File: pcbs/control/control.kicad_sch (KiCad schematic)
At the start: 57 parts, among them J2 USB4125-GF-A-0190, J3 Conn_01x10_Pin, J4 Conn_02x04_Odd_Even, Q1 PMV35EPER, Q10 DMN2020LSN-7, Q2 PMV35EPER, Q3 PMV35EPER, Q4 PMV35EPER, Q5 DMN2020LSN-7, Q6 DMN2020LSN-7, Q7 DMN2020LSN-7, Q8 DMN2020LSN-7, Q9 DMN2020LSN-7, SW1 Sparkle Btn, SW2 Time Adj Btn, U1 DS18B20U, U2 DS3231MZ, U3 TPS259620, U6 ATmega328PB-A

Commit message: pcb and enclosure update
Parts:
- removed BT1: 3000TR, Clock:BAT_3000TR, symbol Clock:3000TR
- added J1: Conn_01x02_Pin, Connector_JST:JST_PH_S2B-PH-SM4-TB_1x02-1MP_P2.00mm_Horizontal, symbol Connector:Conn_01x02_Pin
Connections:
- net GNDD: now also J1.1 (Pin_1)
- net RTC_BAT: now also J1.2 (Pin_2)

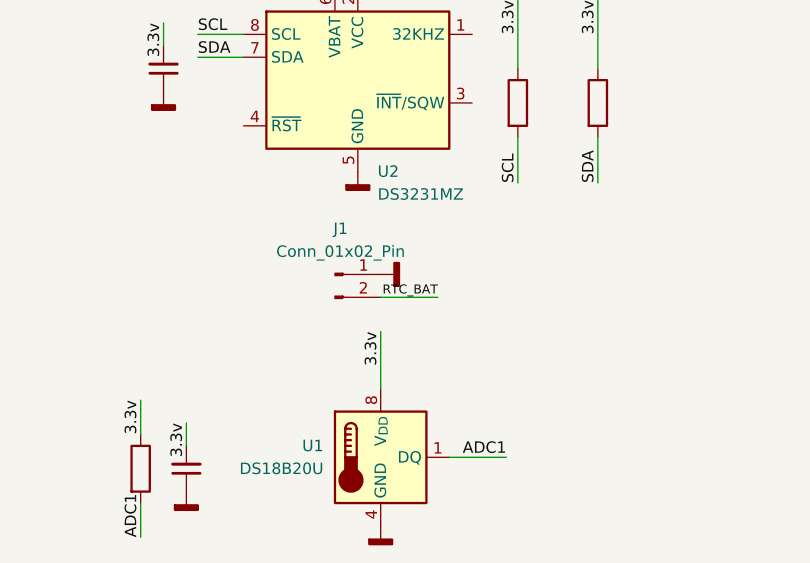
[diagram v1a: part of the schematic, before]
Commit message: lengthened display cable
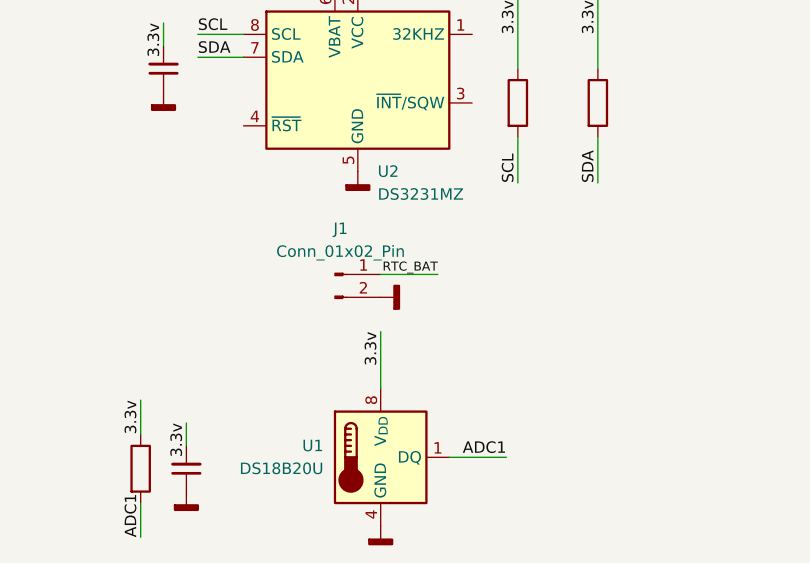
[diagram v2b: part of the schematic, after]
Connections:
- net GNDD: now also J1.2 (Pin_2); no longer J1.1 (Pin_1)
- net RTC_BAT: now also J1.1 (Pin_1); no longer J1.2 (Pin_2)
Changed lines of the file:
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@@
 	(wire
 		(pts
-			(xy 41.91 158.75) (xy 46.99 158.75)
+			(xy 127 153.67) (xy 133.35 153.67)
 		)
 		(stroke
@@
 	(wire
 		(pts
-			(xy 78.74 39.37) (xy 78.74 41.91)
+			(xy 41.91 158.75) (xy 46.99 158.75)
 		)
 		(stroke
@@
 	(wire
 		(pts
-			(xy 137.16 91.44) (xy 143.51 91.44)
+			(xy 78.74 39.37) (xy 78.74 41.91)
 		)
 		(stroke
@@
 	(wire
 		(pts
-			(xy 186.69 66.04) (xy 189.23 66.04)
+			(xy 137.16 91.44) (xy 143.51 91.44)
 		)
 		(stroke
@@
 	(wire
 		(pts
-			(xy 124.46 114.3) (xy 124.46 121.92)
+			(xy 186.69 66.04) (xy 189.23 66.04)
 		)
 		(stroke
@@
 	(wire
 		(pts
-			(xy 127 156.21) (xy 133.35 156.21)
+			(xy 124.46 114.3) (xy 124.46 121.92)
 		)
 		(stroke
@@
 		)
 	)
-	(label "RTC_BAT"
-		(at 133.35 156.21 180)
-		(fields_autoplaced yes)
-		(effects
-			(font
-				(size 1 1)
-			)
-			(justify right bottom)
-		)
-	)
 	(label "ADC3"
 		(at 143.51 66.04 180)
@@
 		)
 	)
+	(label "RTC_BAT"
+		(at 133.35 153.67 180)
+		(fields_autoplaced yes)
+		(effects
+			(font
+				(size 1 1)
+			)
+			(justify right bottom)
+		)
+	)
 	(label "5v"
 		(at 82.55 109.22 270)
@@
 	)
 	(symbol
-		(lib_id "power:GNDD")
-		(at 127 153.67 90)
-		(unit 1)
-		(exclude_from_sim no)
-		(in_bom yes)
-		(on_board yes)
-		(dnp no)
-		(fields_autoplaced yes)
-		(property "Reference" "#PWR026"
-			(at 133.35 153.67 0)
-			(effects
-				(font
-					(size 1.27 1.27)
-				)
-				(hide yes)
-			)
-		)
-		(property "Value" "GNDD"
-			(at 130.81 153.67 0)
-			(effects
-				(font
-					(size 1.27 1.27)
-				)
-				(hide yes)
-			)
-		)
-		(property "Footprint" ""
-			(at 127 153.67 0)
-			(effects
-				(font
-					(size 1.27 1.27)
-				)
-				(hide yes)
-			)
-		)
-		(property "Datasheet" ""
-			(at 127 153.67 0)
-			(effects
-				(font
-					(size 1.27 1.27)
-				)
-				(hide yes)
-			)
-		)
-		(property "Description" "Power symbol creates a global label with name \"GNDD\" , digital ground"
-			(at 127 153.67 0)
-			(effects
-				(font
-					(size 1.27 1.27)
-				)
-				(hide yes)
-			)
-		)
-		(pin "1"
-		)
-		(instances
-			(project "control"
-				(path "/6120ad7c-5b3a-4aa8-9b13-74a3f0996cb1"
-					(reference "#PWR026")
-					(unit 1)
-				)
-			)
-		)
-	)
-	(symbol
 		(lib_id "Device:C_Small")
 		(at 82.55 114.3 180)
@@
 					(unit 1)
 				)
+			)
+		)
+	)
+	(symbol
+		(lib_id "power:GNDD")
+		(at 127 156.21 90)
+		(unit 1)
+		(exclude_from_sim no)
+		(in_bom yes)
+		(on_board yes)
+		(dnp no)
+		(fields_autoplaced yes)
+		(property "Reference" "#PWR026"
+			(at 133.35 156.21 0)
+			(effects
+				(font
+					(size 1.27 1.27)
+				)
+				(hide yes)
+			)
+		)
+		(property "Value" "GNDD"
+			(at 130.81 156.21 0)
+			(effects
+				(font
+					(size 1.27 1.27)
+				)
+				(hide yes)
+			)
+		)
+		(property "Footprint" ""
+			(at 127 156.21 0)
+			(effects
+				(font
+					(size 1.27 1.27)
+				)
+				(hide yes)
+			)
+		)
+		(property "Datasheet" ""
+			(at 127 156.21 0)
+			(effects
+				(font
+					(size 1.27 1.27)
+				)
+				(hide yes)
+			)
+		)
+		(property "Description" "Power symbol creates a global label with name \"GNDD\" , digital ground"
+			(at 127 156.21 0)
+			(effects
+				(font
+					(size 1.27 1.27)
+				)
+				(hide yes)
+			)
+		)
+		(pin "1"
+		)
+		(instances
+			(project "control"
+				(path "/6120ad7c-5b3a-4aa8-9b13-74a3f0996cb1"
+					(reference "#PWR026")
+					(unit 1)
+				)

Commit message: rv-3028 board
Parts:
- removed J1: Conn_01x02_Pin, Connector_JST:JST_PH_S2B-PH-SM4-TB_1x02-1MP_P2.00mm_Horizontal, symbol Connector:Conn_01x02_Pin
- removed R19: 500, Resistor_SMD:R_0805_2012Metric, symbol Device:R
- removed R21, R22: 400k, Resistor_SMD:R_0805_2012Metric, symbol Device:R
- removed U2: DS3231MZ, Package_SO:SOIC-8_3.9x4.9mm_P1.27mm, symbol Timer_RTC:DS3231MZ
- removed U3: TPS259620, Clock:IC_TPS259621DDAT, symbol Clock:TPS259621DDAT
- added C8, C9: FC0V224ZFTBR24, Clock:CAPAE1080X550N, symbol Clock:FC0V224ZFTBR24
- added IC1: TPS25944LRVCR, Clock:QFN50P300X400X80-21N, symbol Clock:TPS25944LRVCR
- added R3: 56.2k, Resistor_SMD:R_0805_2012Metric, symbol Device:R
- added R4: 24.9k, Resistor_SMD:R_0805_2012Metric, symbol Device:R
- added R5: 8.45k, Resistor_SMD:R_0805_2012Metric, symbol Device:R
- added R6: 110k, Resistor_SMD:R_0805_2012Metric, symbol Device:R
- added U2: RV-3028-C7_32.768KHZ_1PPM-TA-QC, Clock:IC_RV-3028-C7_32.768KHZ_1PPM-TA-QC, symbol Clock:RV-3028-C7_32.768KHZ_1PPM-TA-QC
- D1: value LED -> Status LED (Amber)
- F1, F2, F3, F4, F5, F6: value 0.375 A -> 375 mA
- R9: renamed from R18; value 60 -> 300
- renumbered C4 to C1, C1 to C2, C6 to C3, C5 to C4, C8 to C5, C3 to C6, C2 to C7, J3 to J1, J4 to J3, Q6 to Q10, Q10 to Q6, Q9 to Q7, Q7 to Q9, R15 to R1, R11 to R10, R12 to R11, R1 to R12, R2 to R13, R3 to R14, R4 to R15, R5 to R16, R10 to R17, R9 to R18, R8 to R19, R16 to R2, R7 to R20, R6 to R21, R20 to R22, R17 to R23, R14 to R7, R13 to R8, U6 to U1, D5 to U3, U1 to U4
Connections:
- net 3.3v: now also U2.7 (VDD)
- net 5v: now also IC1.4 (OUT_1), IC1.5 (OUT_2), IC1.6 (OUT_3), IC1.7 (OUT_4), IC1.8 (OUT_5)
- net ADC2: now also R9.1; no longer R9.2
- net GNDD: now also C8.2 (-), C9.2 (-), IC1.16 (GND), IC1.21 (EP), R3.1, R4.1, U2.5 (VSS), U2.8 (EVI)
- net SCL: now also U2.3 (SCL)
- net SDA: now also U2.4 (SDA)
- net VBUS: now also IC1.10 (IN_2), IC1.11 (IN_3), IC1.12 (IN_4), IC1.13 (IN_5), IC1.9 (IN_1), R6.1
- net at D1.2 (A): now also R9.2; no longer R9.1
- new net: IC1.15 (OVP), R4.2, R5.1
- new net: IC1.17 (ILIM), R3.2
- new net: C8.1 (+), C9.1 (+), U2.6 (VBACKUP)
- new net: IC1.14 (EN), R5.2, R6.2
- no-connect marks 0 -> 14
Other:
- note added: "1.1"
- note added: "Oct 2025"
- note added: "paper sunshine clock control board"
- moved on the sheet: D1, J2, J3, SW1, SW2, U1, U3, U4
